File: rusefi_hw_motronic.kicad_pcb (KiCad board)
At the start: 2 copper layers, 160 x 135 mm, 50 parts, among them J1 OMEGA PCC_SMP_K, J10 Conn_01x02_Female, J2 Conn_01x02_Female, J3 Conn_01x03_Female, J4 Conn_01x03_Female, J5 Conn_01x03_Female, J6 Conn_01x03_Female, J7 Conn_01x03_Female, J8 Conn_01x04_Female, J9 Conn_01x03_Female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

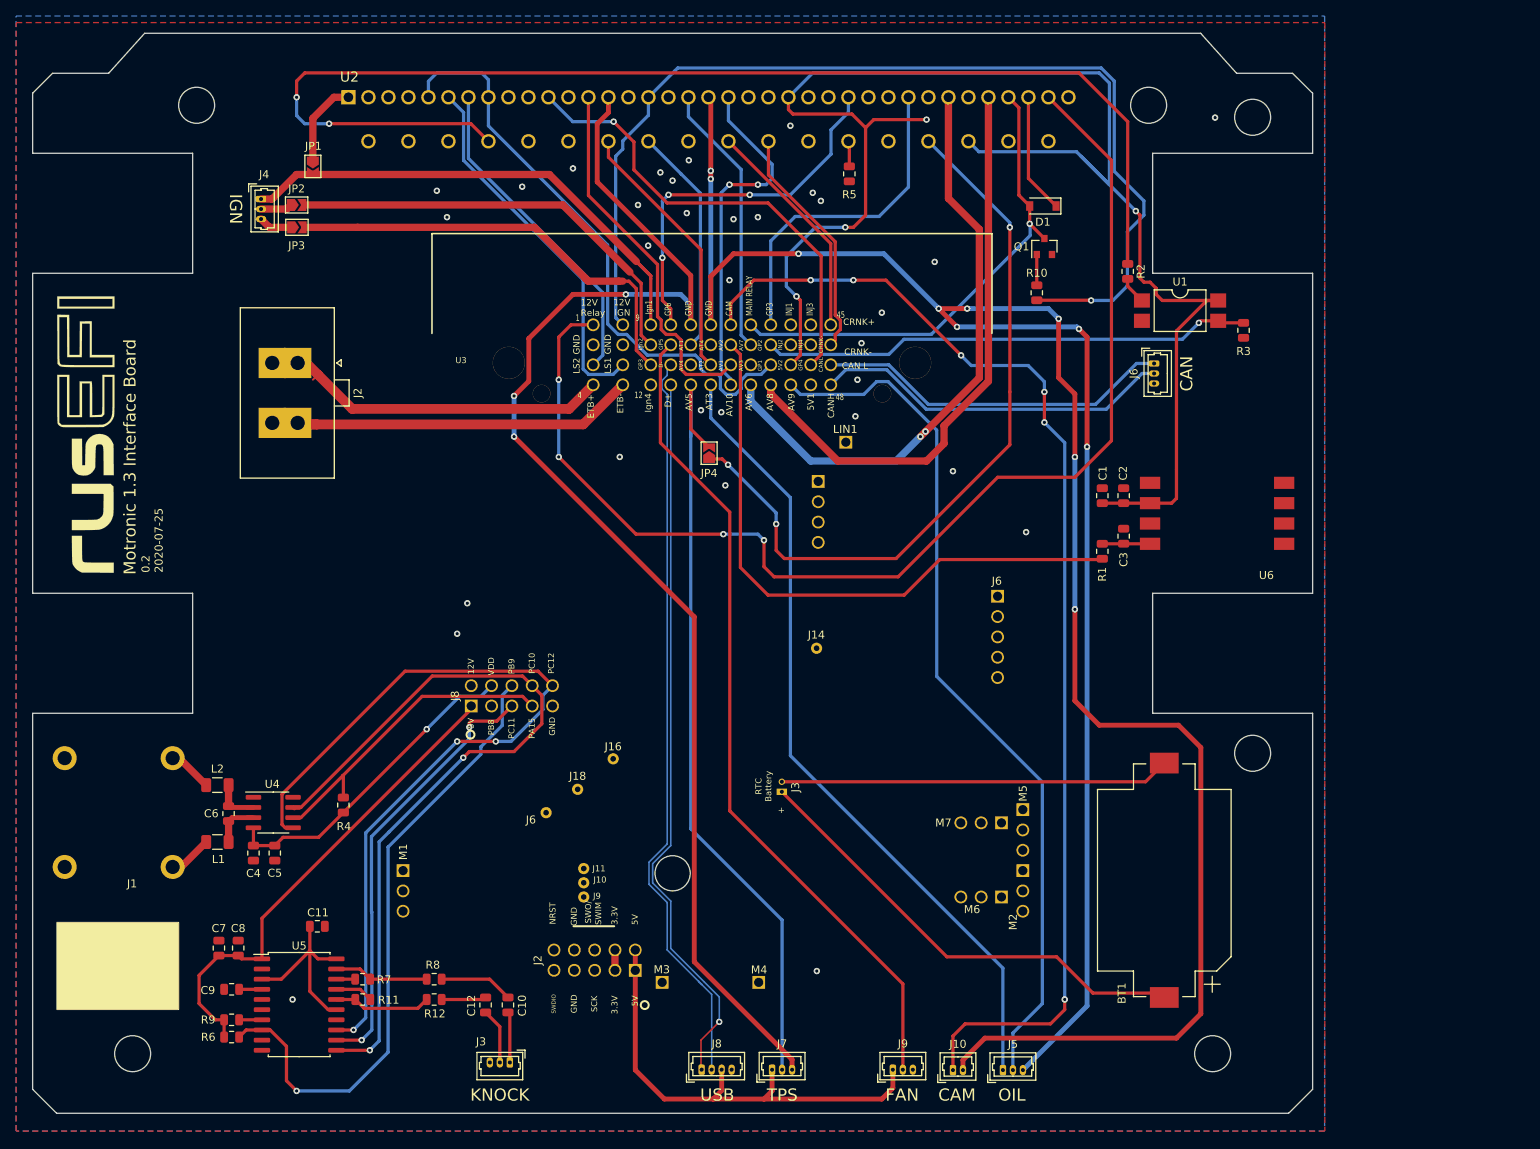
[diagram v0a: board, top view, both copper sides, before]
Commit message: new pcb outline
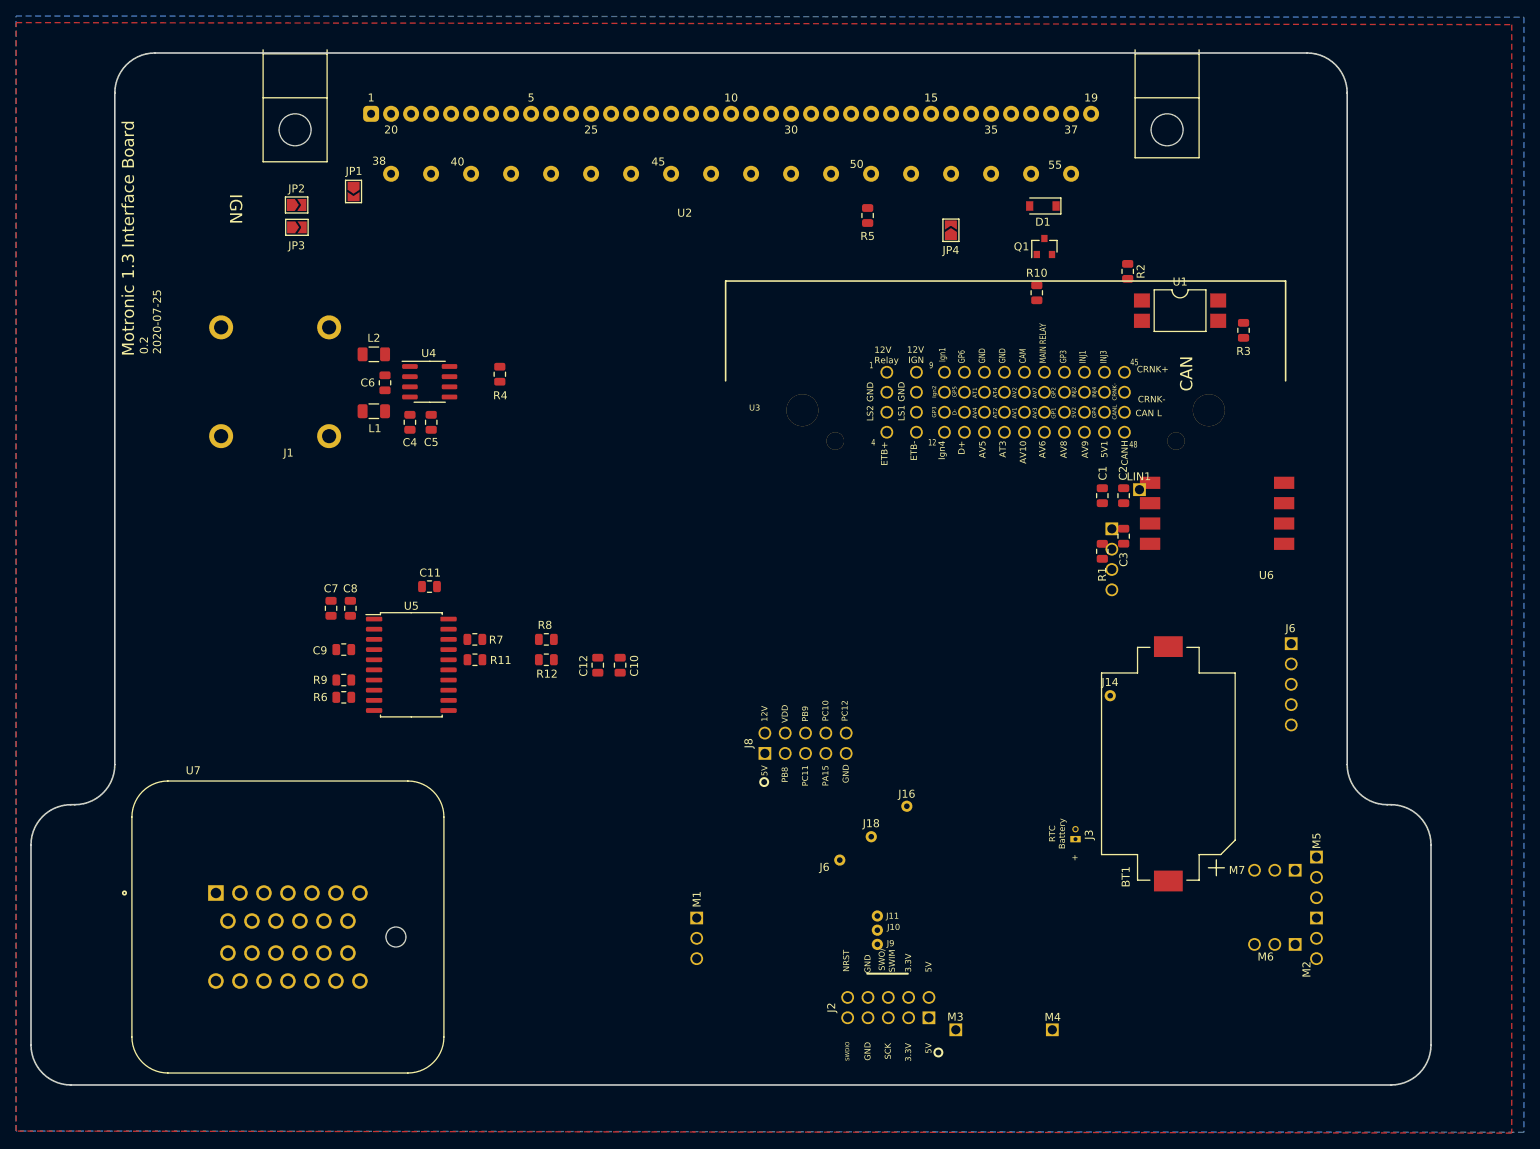
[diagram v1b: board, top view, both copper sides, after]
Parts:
- removed G***: LOGO, rusefi_motronic:rusefi_logo
- removed J10: Conn_01x02_Female, Connector_Molex:Molex_PicoBlade_53047-0210_1x02_P1.25mm_Vertical
- removed J2: Conn_01x02_Female, Connector_Molex:Molex_Sabre_43160-0102_1x02_P7.49mm_Vertical
- removed J3, J4, J5, J6, J7, J9: Conn_01x03_Female, Connector_Molex:Molex_PicoBlade_53047-0310_1x03_P1.25mm_Vertical
- removed J8: Conn_01x04_Female, Connector_Molex:Molex_PicoBlade_53047-0410_1x04_P1.25mm_Vertical
- added U7: TE_6437288-6, rusefi_hw_motronic:TE_6437288-6, F.Cu at (55.3, 138.2)
- U2: value Val** -> BOSCH_55P; footprint rusefi_hw_motronic:BOSCH_55P -> hw_55_te:TE_963063-2
- moved C4 57.3 mm to (70.5, 73.9)
- moved C5 57.3 mm to (73.2, 73.9)
- moved C6 57.3 mm to (67.4, 69.0)
- moved J1 57.3 mm to (60.5, 68.8)
- moved L1 57.3 mm to (66.0, 72.5)
- moved L2 57.3 mm to (66.0, 65.4)
- moved R4 57.3 mm to (81.8, 67.9)
- moved U4 57.3 mm to (73.0, 68.8)
- moved U2 48.2 mm to (110.7, 27.3), turned to 0 degrees
- moved R11 44.7 mm to (78.7, 103.6)
- moved R12 44.7 mm to (87.6, 103.6)
- moved C7 44.7 mm to (60.7, 97.2)
- moved C9 44.7 mm to (62.3, 102.3)
- moved R6 44.7 mm to (62.3, 108.3)
- moved R9 44.7 mm to (62.3, 106.1)
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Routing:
- net SENSOR_GND: track 497.3 -> 0.00 mm, vias 14 -> 0
- net +5V: track 320.8 -> 0.00 mm, vias 4 -> 0
- net AC_ON_INPUT: track 154.2 -> 0.00 mm, vias 2 -> 0
- net +12V: track 150.4 -> 0.00 mm, vias 4 -> 0
- net CAM: track 147.5 -> 0.00 mm, vias 6 -> 0
- net IGN_SWITCH: track 131.0 -> 0.00 mm, vias 1 -> 0
- net OIL_PRESSURE: track 108.9 -> 0.00 mm
- net SCK: track 105.7 -> 0.00 mm, vias 3 -> 0
- net FAN_PWM: track 103.7 -> 0.00 mm
- net OIL_TEMP: track 100.8 -> 0.00 mm
- net MISO: track 100.1 -> 0.00 mm, vias 2 -> 0
- net TPS: track 99.9 -> 0.00 mm
- net USB-: track 93.6 -> 0.00 mm
- net Net-(JP4-Pad1): track 93.5 -> 0.00 mm, vias 3 -> 0
- net USB+: track 91.0 -> 0.00 mm, vias 1 -> 0
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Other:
- board size 160 x 135 mm -> 175 x 129 mm
- board text removed: "CAM"
- board text removed: "FAN"
- board text removed: "KNOCK"
- board text removed: "OIL"
- board text removed: "TPS"
- board text removed: "USB"

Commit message: getting closer...
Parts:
- added G***: LOGO, rusefi_motronic:rusefi_logo, F.Cu at (39.1, 50.8)
- moved C10 24.7 mm to (80.2, 122.5), turned to 180 degrees
- moved C12 20.8 mm to (80.2, 119.7), turned to 180 degrees
- moved J1 18.2 mm to (51.7, 84.8)
- moved L1 17.2 mm to (58.1, 87.8)
- moved C4 17.2 mm to (62.6, 89.1)
- moved L2 17.2 mm to (58.1, 80.6)
- moved C5 17.2 mm to (65.3, 89.1)
- moved C6 17.2 mm to (59.5, 84.2)
- moved R4 17.2 mm to (73.9, 83.1)
- moved U4 17.2 mm to (65.1, 84.1)
- moved R8 13.0 mm to (83.4, 113.3), turned to 270 degrees
- moved R12 11.8 mm to (80.9, 113.3), turned to 270 degrees
- moved C1 8.58 mm to (161.7, 90.3)
- moved C2 8.44 mm to (164.1, 90.3)
- moved U6 8.42 mm to (184.2, 88.7)
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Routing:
- net SENSOR_GND: track 0.00 -> 206.7 mm
- net IGN1: track 0.00 -> 185.2 mm, vias 0 -> 1
- net ETB+: track 0.00 -> 98.9 mm
- net ETB-: track 0.00 -> 98.8 mm
- net IGN2: track 0.00 -> 95.3 mm
- net AC_ON_INPUT: track 0.00 -> 89.9 mm
- net IGN_C: track 0.00 -> 89.3 mm, vias 0 -> 1
- net IGN_B: track 0.00 -> 88.6 mm
- net IGN3: track 0.00 -> 88.2 mm, vias 0 -> 2
- net IAC_OPEN: track 0.00 -> 77.1 mm, vias 0 -> 1
- net IAC_CLOSE: track 0.00 -> 76.3 mm
- net IGN_SWITCH: track 0.00 -> 71.2 mm, vias 0 -> 1
- net AC_IDLE_IN: track 0.00 -> 27.8 mm
- net KNOCK_2: track 0.00 -> 26.7 mm
- net KNOCK_1: track 0.00 -> 25.1 mm
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
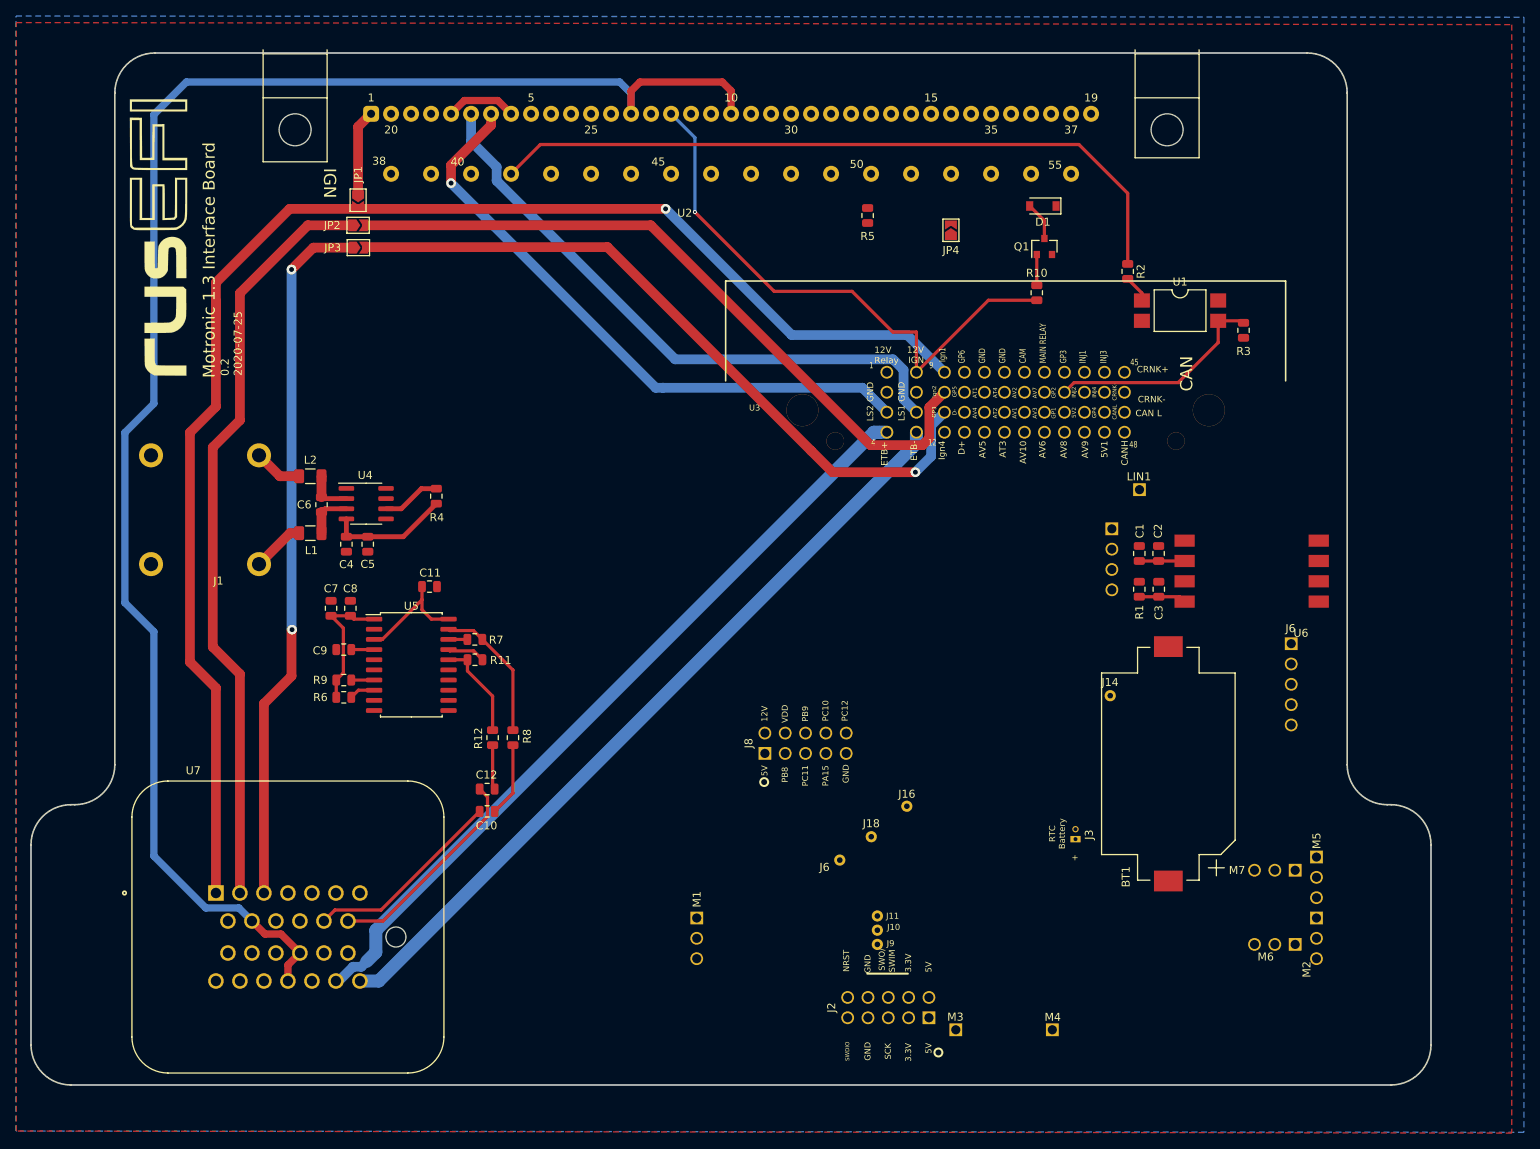
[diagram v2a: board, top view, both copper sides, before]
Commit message: finished routing first pass
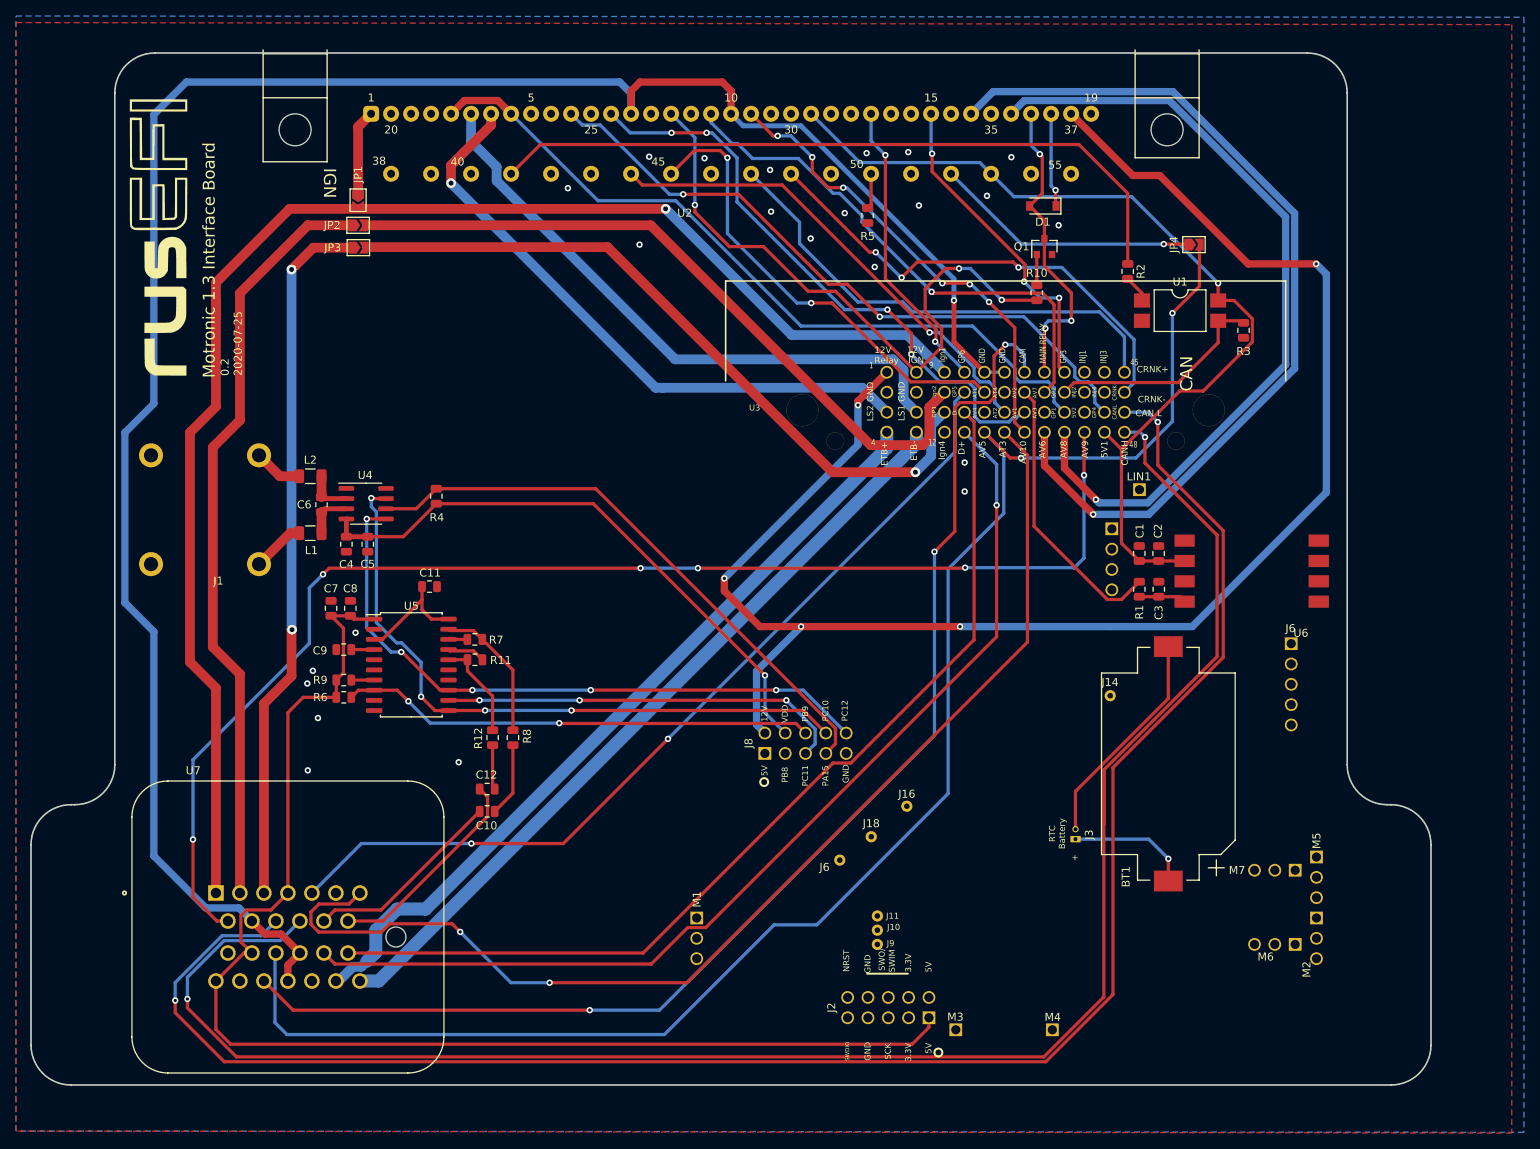
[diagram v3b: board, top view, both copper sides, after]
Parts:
- moved JP4 30.4 mm to (168.6, 51.7), turned to 0 degrees
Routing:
- net +5V: track 22.4 -> 277.8 mm, vias 0 -> 1
- net CAN_H: track 0.00 -> 230.3 mm, vias 0 -> 2
- net CAN_L: track 0.00 -> 228.1 mm, vias 0 -> 2
- net TPS: track 0.00 -> 205.3 mm, vias 0 -> 2
- net +12V: track 0.00 -> 203.4 mm, vias 0 -> 5
- net OIL_PRESSURE: track 0.00 -> 164.4 mm, vias 0 -> 6
- net CAM: track 0.00 -> 159.2 mm, vias 0 -> 3
- net OIL_TEMP: track 0.00 -> 147.2 mm, vias 0 -> 2
- net USB+: track 0.00 -> 128.8 mm, vias 0 -> 1
- net USB-: track 0.00 -> 123.4 mm
- net INJ_1: track 0.00 -> 112.8 mm, vias 0 -> 1
- net FAN_PWM: track 0.00 -> 111.2 mm, vias 0 -> 2
- net INJ_2: track 0.00 -> 100.6 mm, vias 0 -> 1
- net FUEL_PUMP: track 8.87 -> 95.2 mm
- net TACH_OUT: track 0.00 -> 83.8 mm, vias 0 -> 2
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
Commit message: cleaned up routing
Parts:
- added J2: Conn_01x02_Female, Connector_Molex:Molex_PicoBlade_53047-0210_1x02_P1.25mm_Vertical, F.Cu at (190.6, 132.0)
- moved JP4 36.9 mm to (144.8, 79.9), turned to 180 degrees
- moved R2 2.19 mm to (162.1, 53.8)
- moved G*** 0.06 mm to (39.1, 50.8)
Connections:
- U3 pad J31: RTC_BATT+ -> (no net)
- U3 pad J32: RTC_BATT- -> (no net)
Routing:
- net TPS: track 205.3 -> 157.3 mm, vias 2 -> 1
- net Net-(JP4-Pad1): track 33.3 -> 66.7 mm
- net RTC_BATT+: track 15.4 -> 32.1 mm, vias 1 -> 0
- net RTC_BATT-: track 27.6 -> 41.1 mm
- net Net-(C11-Pad1): track 14.7 -> 24.2 mm
- net CAN_H: track 230.3 -> 239.3 mm
- net CAN_L: track 228.1 -> 236.2 mm
- net OIL_PRESSURE: track 164.4 -> 159.2 mm
- net IAC_OPEN: track 77.1 -> 72.9 mm
- net IAC_CLOSE: track 76.3 -> 77.2 mm
- net VR_N: track 60.1 -> 59.3 mm
- net SENSOR_GND: track 258.9 -> 258.1 mm
- net ECM_RELAY: track 38.8 -> 38.1 mm, vias 3 -> 4
- net GND: vias 23 -> 30
- net CAM: vias 3 -> 2
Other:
- board text added: "RTC"
- board text removed: "CAN"
